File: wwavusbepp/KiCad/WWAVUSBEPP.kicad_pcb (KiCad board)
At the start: 4 copper layers, 36.8 x 40.8 mm, 35 parts, among them J1 USB_B, J2 Conn_01x26_Female, J3 Conn_01x06_Female, J4 Conn_01x04_Male, U1 CY7C68013-56LFC, U2 LT1762-3.3, U3 NCP302LSN45T1G, U4 FM24C64B, X1 24Mhz

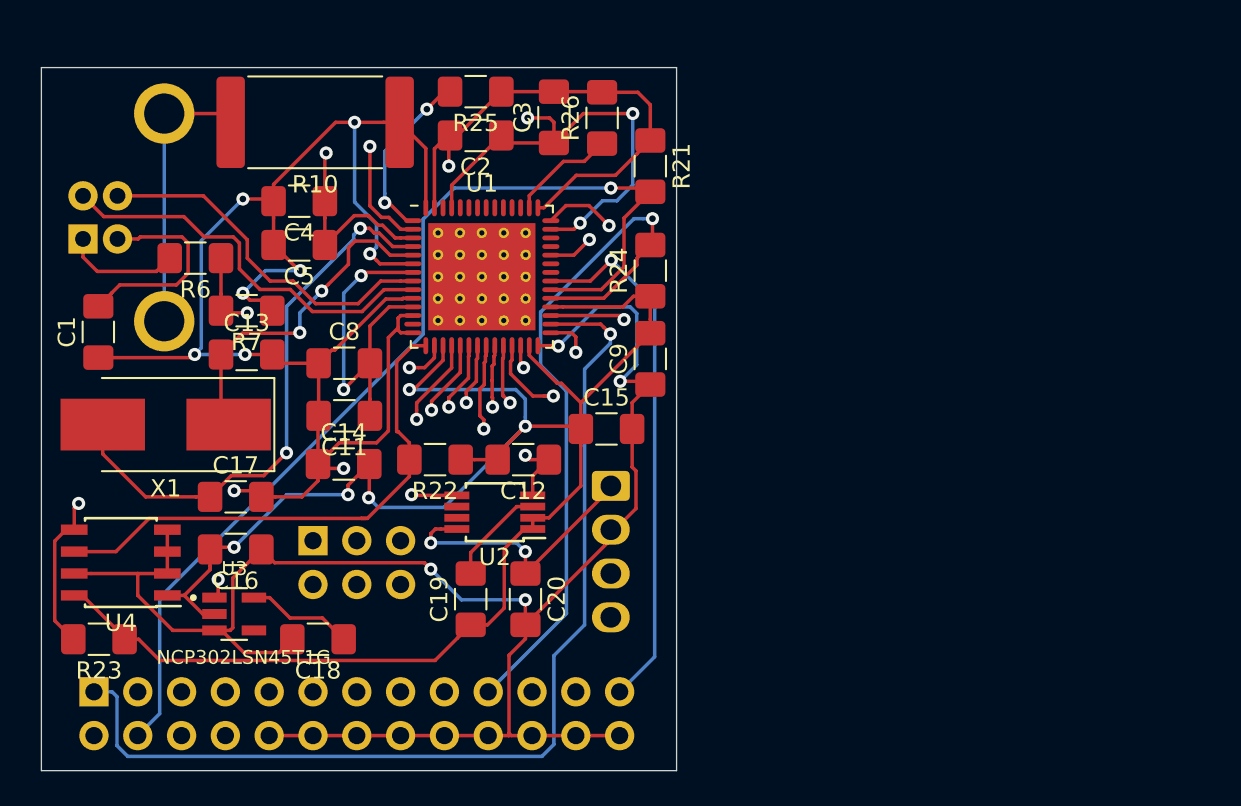
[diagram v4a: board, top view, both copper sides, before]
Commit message: Added testpoints and rerouted some tracks. Work in progress.
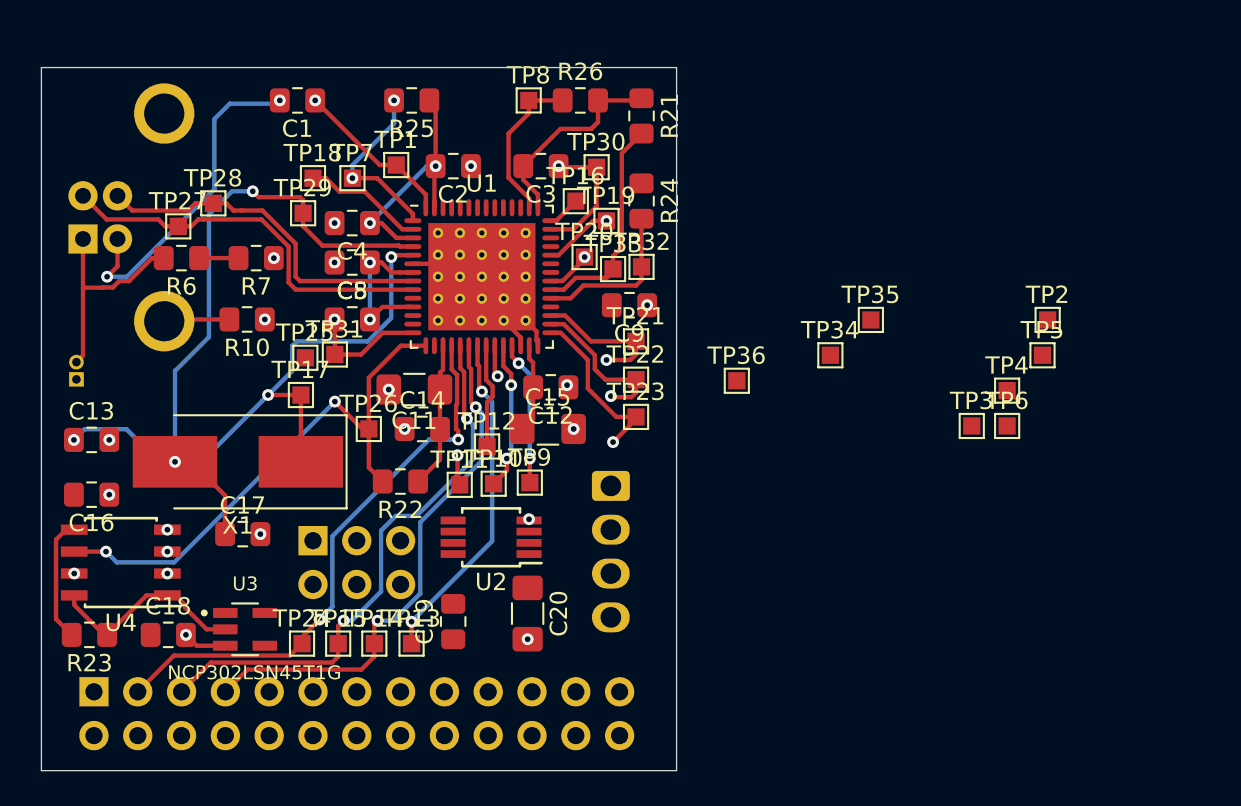
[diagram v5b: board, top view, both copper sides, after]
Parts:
- added J5: Conn_01x02_Male, Connector_PinHeader_1.00mm:PinHeader_1x02_P1.00mm_Vertical, B.Cu at (60.7, 133.5)
- added TP1: TestPoint, TestPoint:TestPoint_Pad_1.0x1.0mm, F.Cu at (79.2, 121.1)
- added TP10: TestPoint, TestPoint:TestPoint_Pad_1.0x1.0mm, F.Cu at (84.9, 139.6)
- added TP11: TestPoint, TestPoint:TestPoint_Pad_1.0x1.0mm, F.Cu at (82.9, 139.6)
- added TP12: TestPoint, TestPoint:TestPoint_Pad_1.0x1.0mm, F.Cu at (84.5, 137.4)
- added TP13: TestPoint, TestPoint:TestPoint_Pad_1.0x1.0mm, F.Cu at (80.1, 148.8)
- added TP14: TestPoint, TestPoint:TestPoint_Pad_1.0x1.0mm, F.Cu at (78.0, 148.8)
- added TP15: TestPoint, TestPoint:TestPoint_Pad_1.0x1.0mm, F.Cu at (75.9, 148.8)
- added TP16: TestPoint, TestPoint:TestPoint_Pad_1.0x1.0mm, F.Cu at (89.7, 123.2)
- added TP17: TestPoint, TestPoint:TestPoint_Pad_1.0x1.0mm, F.Cu at (73.7, 134.4)
- added TP18: TestPoint, TestPoint:TestPoint_Pad_1.0x1.0mm, F.Cu at (74.4, 121.9)
- added TP19: TestPoint, TestPoint:TestPoint_Pad_1.0x1.0mm, F.Cu at (91.4, 124.3)
- added TP2: TestPoint, TestPoint:TestPoint_Pad_1.0x1.0mm, F.Cu at (117.0, 130.1)
- added TP20: TestPoint, TestPoint:TestPoint_Pad_1.0x1.0mm, F.Cu at (90.2, 126.4)
- added TP21: TestPoint, TestPoint:TestPoint_Pad_1.0x1.0mm, F.Cu at (93.2, 131.3)
- added TP22: TestPoint, TestPoint:TestPoint_Pad_1.0x1.0mm, F.Cu at (93.2, 133.5)
- added TP23: TestPoint, TestPoint:TestPoint_Pad_1.0x1.0mm, F.Cu at (93.2, 135.7)
- added TP24: TestPoint, TestPoint:TestPoint_Pad_1.0x1.0mm, F.Cu at (73.8, 148.8)
- added TP25: TestPoint, TestPoint:TestPoint_Pad_1.0x1.0mm, F.Cu at (74.0, 132.3)
- added TP26: TestPoint, TestPoint:TestPoint_Pad_1.0x1.0mm, F.Cu at (77.7, 136.4)
- added TP27: TestPoint, TestPoint:TestPoint_Pad_1.0x1.0mm, F.Cu at (66.6, 124.7)
- added TP28: TestPoint, TestPoint:TestPoint_Pad_1.0x1.0mm, F.Cu at (68.6, 123.3)
- added TP29: TestPoint, TestPoint:TestPoint_Pad_1.0x1.0mm, F.Cu at (73.9, 123.9)
- added TP3: TestPoint, TestPoint:TestPoint_Pad_1.0x1.0mm, F.Cu at (112.6, 136.2)
- added TP30: TestPoint, TestPoint:TestPoint_Pad_1.0x1.0mm, F.Cu at (90.9, 121.2)
- added TP31: TestPoint, TestPoint:TestPoint_Pad_1.0x1.0mm, F.Cu at (75.7, 132.1)
- added TP32: TestPoint, TestPoint:TestPoint_Pad_1.0x1.0mm, F.Cu at (93.5, 127.0)
- added TP33: TestPoint, TestPoint:TestPoint_Pad_1.0x1.0mm, F.Cu at (91.8, 127.1)
- added TP34: TestPoint, TestPoint:TestPoint_Pad_1.0x1.0mm, F.Cu at (104.4, 132.1)
- added TP35: TestPoint, TestPoint:TestPoint_Pad_1.0x1.0mm, F.Cu at (106.8, 130.1)
- added TP36: TestPoint, TestPoint:TestPoint_Pad_1.0x1.0mm, F.Cu at (99.0, 133.6)
- added TP4: TestPoint, TestPoint:TestPoint_Pad_1.0x1.0mm, F.Cu at (114.7, 134.2)
- added TP5: TestPoint, TestPoint:TestPoint_Pad_1.0x1.0mm, F.Cu at (116.7, 132.1)
- added TP6: TestPoint, TestPoint:TestPoint_Pad_1.0x1.0mm, F.Cu at (114.7, 136.2)
- added TP7: TestPoint, TestPoint:TestPoint_Pad_1.0x1.0mm, F.Cu at (76.7, 121.9)
- added TP8: TestPoint, TestPoint:TestPoint_Pad_1.0x1.0mm, F.Cu at (86.9, 117.3)
- added TP9: TestPoint, TestPoint:TestPoint_Pad_1.0x1.0mm, F.Cu at (87.0, 139.5)
- C1, C12, C13, C14, C16, C17, C18, C19, C2, C3, C4, C5, C8, C9: footprint Capacitor_SMD:C_1206_3216Metric_Pad1.42x1.75mm_HandSolder -> Capacitor_SMD:C_0805_2012Metric_Pad1.15x1.40mm_HandSolder
- R10: footprint Resistor_SMD:R_4020_10251Metric_Pad1.65x5.30mm_HandSolder -> Resistor_SMD:R_0805_2012Metric_Pad1.15x1.40mm_HandSolder
- R21, R23, R25, R26: footprint Resistor_SMD:R_1206_3216Metric_Pad1.42x1.75mm_HandSolder -> Resistor_SMD:R_0805_2012Metric_Pad1.15x1.40mm_HandSolder
- R22: value 10k -> 2.2k; footprint Resistor_SMD:R_1206_3216Metric_Pad1.42x1.75mm_HandSolder -> Resistor_SMD:R_0805_2012Metric_Pad1.15x1.40mm_HandSolder
- R24: value 2.2k -> 10k; footprint Resistor_SMD:R_1206_3216Metric_Pad1.42x1.75mm_HandSolder -> Resistor_SMD:R_0805_2012Metric_Pad1.15x1.40mm_HandSolder
- R6: value R_US -> 15.1k; footprint Resistor_SMD:R_1206_3216Metric_Pad1.42x1.75mm_HandSolder -> Resistor_SMD:R_0805_2012Metric_Pad1.15x1.40mm_HandSolder
- R7: value R_US -> 5.1k; footprint Resistor_SMD:R_1206_3216Metric_Pad1.42x1.75mm_HandSolder -> Resistor_SMD:R_0805_2012Metric_Pad1.15x1.40mm_HandSolder
- moved C1 17.7 mm to (73.5, 117.3), turned to 180 degrees
- moved R10 12.1 mm to (70.6, 130.0)
- moved C13 10.3 mm to (61.6, 137.0)
- moved C16 8.94 mm to (61.6, 140.2)
- moved C18 8.69 mm to (66.0, 148.3), turned to 0 degrees
- moved C14 4.99 mm to (80.8, 136.4)
- moved X1 4.71 mm to (70.1, 138.3)
- moved C12 4.48 mm to (88.2, 134.0)
- moved C11 4.34 mm to (80.3, 134.1)
- moved R24 4.07 mm to (93.5, 123.2), turned to 270 degrees
- moved R25 3.75 mm to (80.1, 117.3)
- moved C15 3.39 mm to (88.0, 136.4)
- moved C9 3.34 mm to (92.8, 129.2), turned to 180 degrees
- moved C4 3.33 mm to (76.7, 124.5)
- moved C5 3.24 mm to (76.7, 126.7)
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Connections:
- U1 pad 57: Net-(U1-Pad57) -> Earth
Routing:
- net Earth: track 267.4 -> 38.4 mm, vias 18 -> 23
- net +3V3: track 200.4 -> 60.8 mm, vias 9 -> 4
- net 1: track 59.0 -> 9.10 mm
- net U3_R: track 51.4 -> 1.92 mm, vias 2 -> 0
- net Net-(J2-Pad4): track 60.6 -> 12.7 mm, vias 1 -> 0
- net 8: track 51.8 -> 8.16 mm
- net 23: track 49.3 -> 7.02 mm, vias 1 -> 0
- net 2: track 49.2 -> 9.94 mm
- net Net-(J2-Pad21): track 49.2 -> 10.3 mm
- net Net-(J2-Pad19): track 42.1 -> 9.25 mm, vias 1 -> 0
- net SDA: track 34.0 -> 7.19 mm, vias 2 -> 0
- net 11: track 28.1 -> 6.13 mm, vias 1 -> 0
- net Net-(R6-Pad1): track 21.8 -> 2.29 mm, vias 2 -> 0
- net 13: track 26.3 -> 9.18 mm, vias 1 -> 2
- net 17: track 25.4 -> 8.37 mm, vias 1 -> 2
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- added copper zone on In1.Cu, net Earth
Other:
- net class +3V3 added: clearance 0.1524, trace_width 0.254, via_dia 0.6858, via_drill 0.3302
- net class Default: clearance 0.254 -> 0.1524; trace_width 0.2032 -> 0.1524; via_dia 0.762 -> 0.6858; via_drill 0.381 -> 0.3302
- rule trace_clearance: 0.254 -> 0.1524

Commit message: routing complete.
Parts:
- removed TP2, TP3, TP35, TP4, TP5, TP6: TestPoint, TestPoint:TestPoint_Pad_1.0x1.0mm
- J5: footprint Connector_PinHeader_1.00mm:PinHeader_1x02_P1.00mm_Vertical -> Connector_PinHeader_2.00mm:PinHeader_1x02_P2.00mm_Vertical
- moved TP36 21.2 mm to (83.9, 118.6)
- moved TP34 14.8 mm to (89.9, 129.3)
- moved J5 2.25 mm to (62.9, 134.0), turned to 90 degrees
- moved U3 1.65 mm to (70.0, 146.4)
- moved TP32 0.76 mm to (94.2, 127.0)
- moved R24 0.67 mm to (94.1, 123.4)
- moved TP24 0.60 mm to (73.5, 148.3)
- moved TP25 0.43 mm to (73.6, 132.1)
- moved TP13 0.40 mm to (79.8, 148.7)
- moved TP14 0.40 mm to (77.6, 148.7)
- moved TP33 0.38 mm to (92.2, 127.1)
- moved C18 0.37 mm to (65.8, 148.0), turned to 180 degrees
- moved TP15 0.32 mm to (75.6, 148.8)
- moved TP30 0.27 mm to (91.1, 121.0)
- moved TP19 0.25 mm to (91.7, 124.3)
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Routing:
- net +3V3: track 60.8 -> 154.0 mm, vias 4 -> 13
- net Net-(J2-Pad4): track 12.7 -> 75.0 mm, vias 0 -> 1
- net 23: track 7.02 -> 65.3 mm, vias 0 -> 1
- net 1: track 9.10 -> 62.2 mm
- net Net-(J2-Pad21): track 10.3 -> 58.3 mm
- net Net-(C20-Pad1): track 0.00 -> 46.8 mm, vias 0 -> 3
- net U3_R: track 1.92 -> 43.8 mm, vias 0 -> 2
- net 2: track 9.94 -> 48.8 mm, vias 1 -> 3
- net 8: track 8.16 -> 46.0 mm
- net Net-(J2-Pad19): track 9.25 -> 40.7 mm, vias 0 -> 2
- net SDA: track 7.19 -> 34.6 mm, vias 0 -> 4
- net Net-(R6-Pad1): track 2.29 -> 25.2 mm, vias 0 -> 3
- net 11: track 6.13 -> 26.8 mm, vias 0 -> 2
- net Net-(J1-Pad5): track 3.82 -> 23.6 mm
- net 13: track 9.18 -> 25.0 mm
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
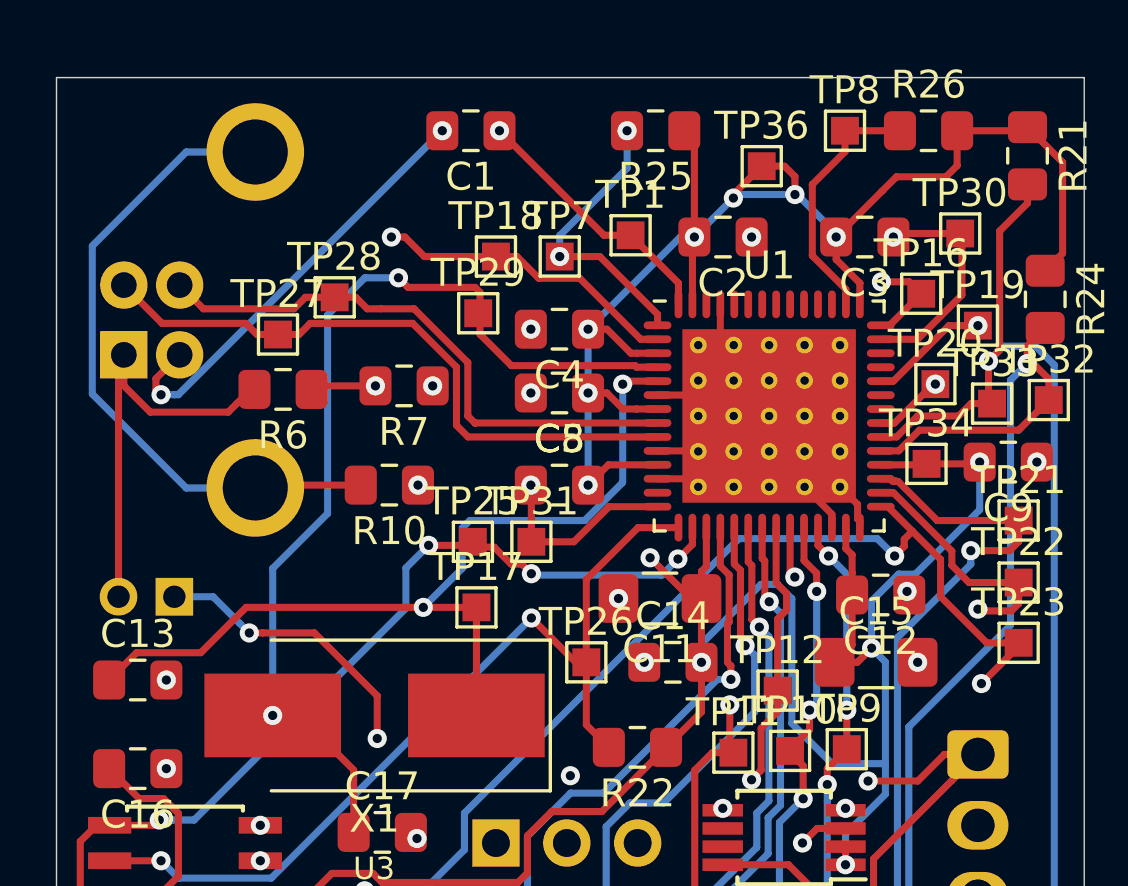
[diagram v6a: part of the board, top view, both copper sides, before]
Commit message: Fixed the R10 resistor footprint and rerouting. No silkscreen changes done.
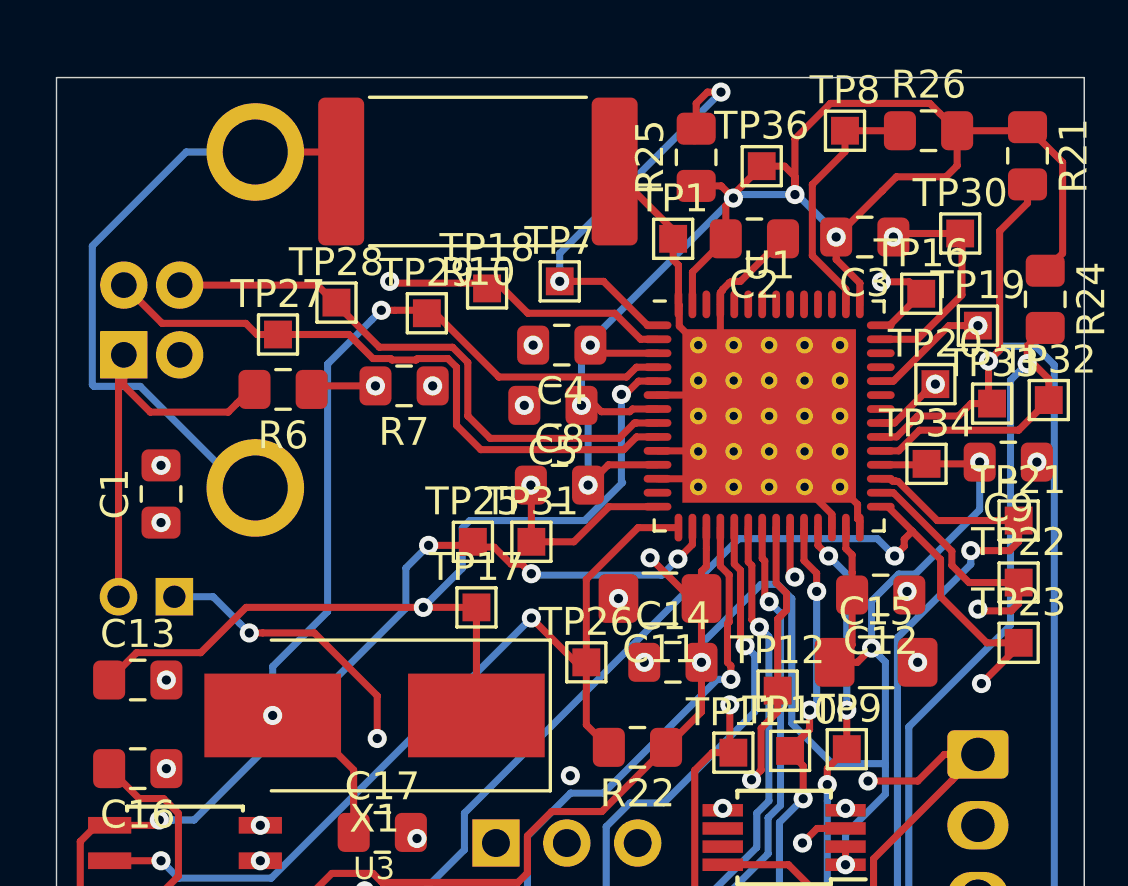
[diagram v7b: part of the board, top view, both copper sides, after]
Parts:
- R10: footprint Resistor_SMD:R_0805_2012Metric_Pad1.15x1.40mm_HandSolder -> Resistor_SMD:R_4020_10251Metric_Pad1.65x5.30mm_HandSolder
- moved C1 17.1 mm to (62.4, 130.4), turned to 90 degrees
- moved R10 11.7 mm to (73.8, 118.8)
- moved TP29 1.84 mm to (71.9, 123.9)
- moved R25 1.74 mm to (81.6, 118.3), turned to 90 degrees
- moved TP1 1.53 mm to (80.8, 121.2)
- moved TP18 1.19 mm to (74.1, 123.0)
- moved C2 1.13 mm to (83.7, 121.2)
- moved TP7 0.89 mm to (76.7, 122.7)
- moved C4 0.58 mm to (76.8, 125.0)
- moved C5 0.50 mm to (76.5, 127.2)
- moved TP28 0.20 mm to (68.7, 123.5)
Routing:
- net Net-(C1-Pad2): track 15.9 -> 4.24 mm, vias 2 -> 1
- net +3V3: track 154.0 -> 161.9 mm, vias 13 -> 12
- net Net-(J2-Pad21): track 58.3 -> 61.1 mm
- net XTALOUT: track 35.7 -> 33.1 mm
- net 23: track 65.3 -> 63.3 mm
- net Earth: track 48.8 -> 50.3 mm, vias 23 -> 21
- net Net-(J1-Pad5): track 23.6 -> 23.1 mm
- net U3_R: track 43.8 -> 44.3 mm

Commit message: Finished routing, silk, etc. Should be complete.
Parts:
- renumbered TP1 to t1, TP10 to t10, TP11 to t11, TP12 to t12, TP13 to t13, TP14 to t14, TP15 to t15, TP16 to t16, TP17 to t17, TP18 to t18, TP19 to t19, TP20 to t20, TP21 to t21, TP22 to t22, TP23 to t23, TP24 to t24, TP25 to t25, TP26 to t26, TP27 to t27, TP28 to t28, TP29 to t29, TP30 to t30, TP31 to t31, TP32 to t32, TP33 to t33, TP34 to t34, TP36 to t36, TP7 to t7, TP8 to t8, TP9 to t9
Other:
- board text added: "wwavusbepp v01 (it wasn't me)"
- board text added: "yusufm@"
